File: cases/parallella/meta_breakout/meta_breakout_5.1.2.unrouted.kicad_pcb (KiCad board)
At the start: 4 copper layers, 97.8 x 71.1 mm, 8 parts, among them J1 BSH-120, J2 Conn_02x30_Odd_Even, J3 Conn_02x30_Odd_Even, J4 Conn_02x30_Odd_Even, J5 Conn_02x30_Odd_Even

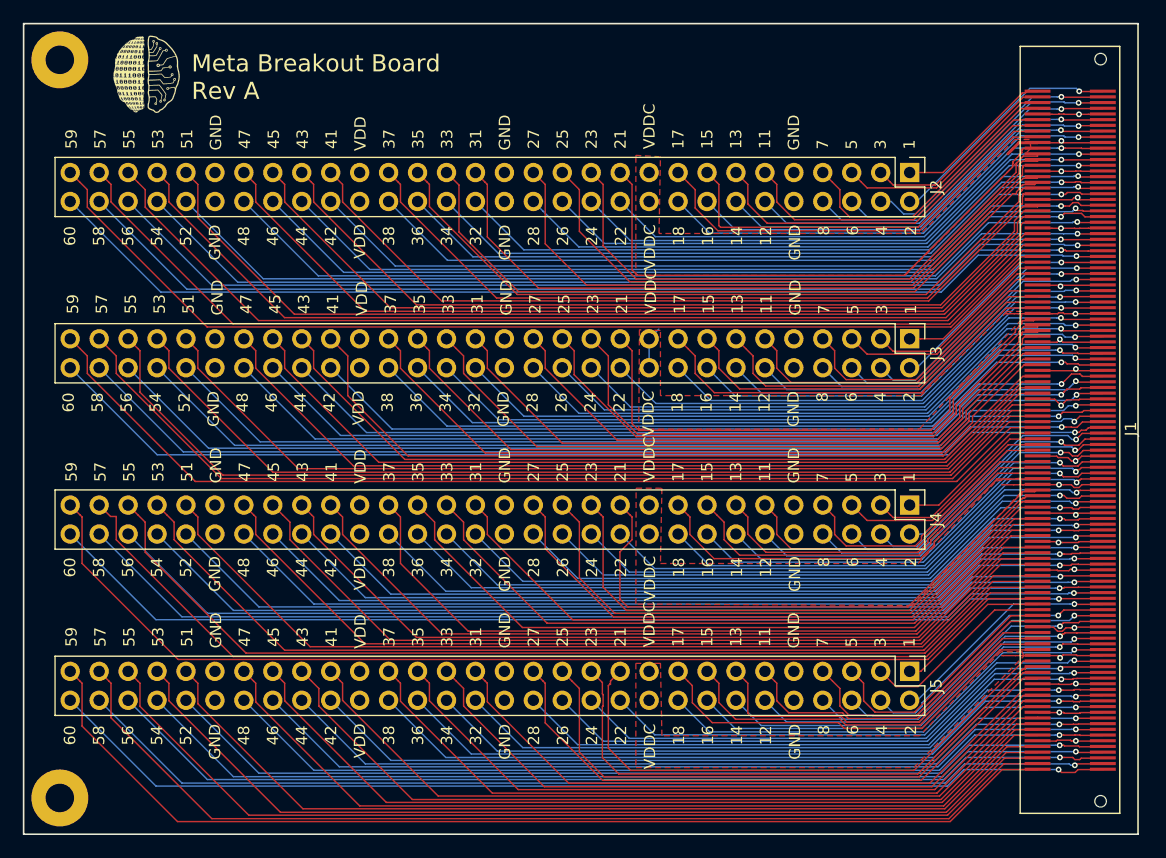
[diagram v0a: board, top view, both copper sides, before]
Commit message: Change parallella files into routed and unrouted ones
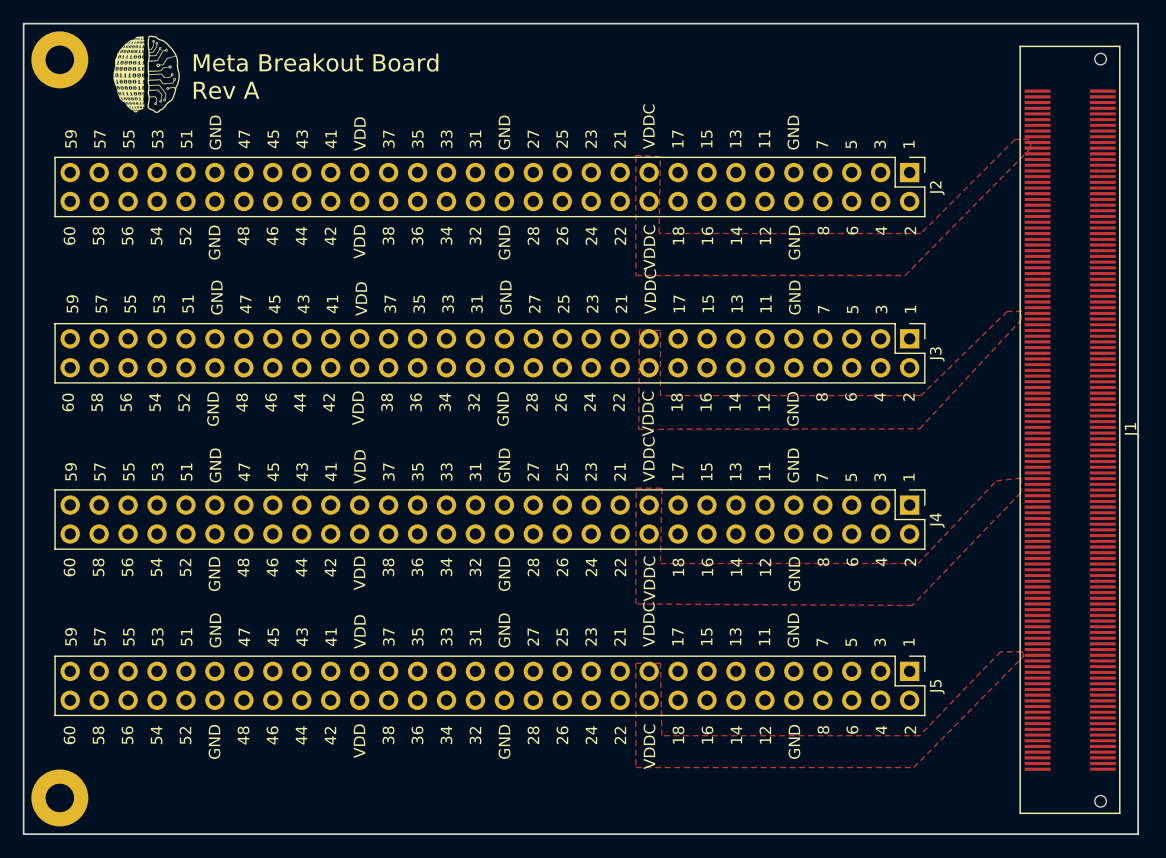
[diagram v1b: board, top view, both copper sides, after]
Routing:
- net /CTRL_OUT0: track 95.3 -> 0.00 mm, vias 1 -> 0
- net /CTRL_IN2: track 95.1 -> 0.00 mm
- net /CTRL_OUT1: track 94.8 -> 0.00 mm, vias 1 -> 0
- net /CTRL_OUT3: track 94.5 -> 0.00 mm, vias 1 -> 0
- net /CTRL_OUT2: track 94.5 -> 0.00 mm, vias 1 -> 0
- net /CTRL_IN3: track 94.4 -> 0.00 mm
- net /CTRL_IN0: track 94.0 -> 0.00 mm
- net /CTRL_IN1: track 92.9 -> 0.00 mm
- net /DATA_OUT_P7: track 92.7 -> 0.00 mm, vias 1 -> 0
- net /DATA_OUT_P15: track 92.2 -> 0.00 mm, vias 1 -> 0
- net /DATA_OUT_P23: track 92.0 -> 0.00 mm, vias 1 -> 0
- net /DATA_OUT_P31: track 91.9 -> 0.00 mm, vias 1 -> 0
- net /DATA_IN_P31: track 91.5 -> 0.00 mm
- net /DATA_IN_P7: track 91.4 -> 0.00 mm
- net /DATA_IN_P23: track 91.4 -> 0.00 mm
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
